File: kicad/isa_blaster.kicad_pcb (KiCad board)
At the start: 2 copper layers, 81.3 x 30.9 mm, 18 parts, among them J1 Bus_ISA_8bit, J2 Conn_02x06_Odd_Even, J3 USB_A, U3 TXS0108EPW, U4 TXS0108EPW, U5 TXS0108EPW, U6 RaspberryPi_Pico

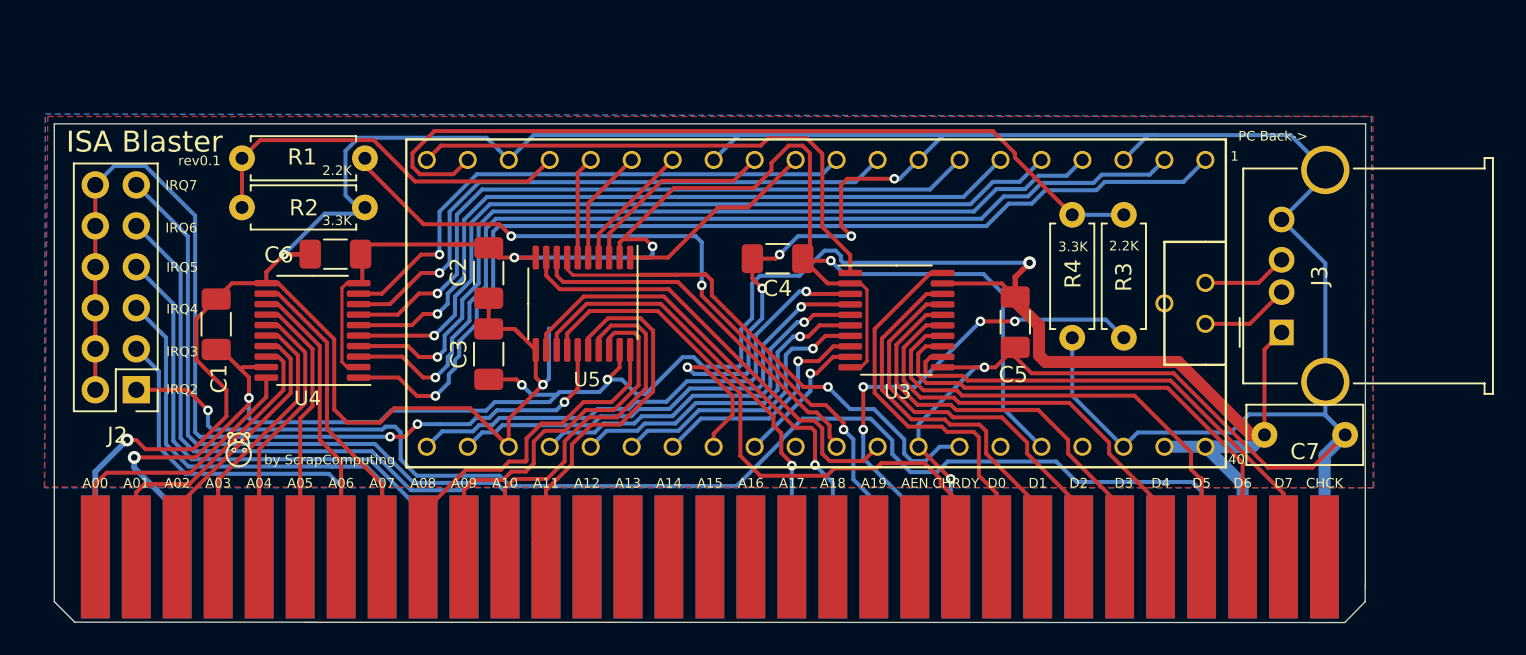
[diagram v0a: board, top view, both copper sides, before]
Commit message: Added RESET circuit, debug header and SMD resistors
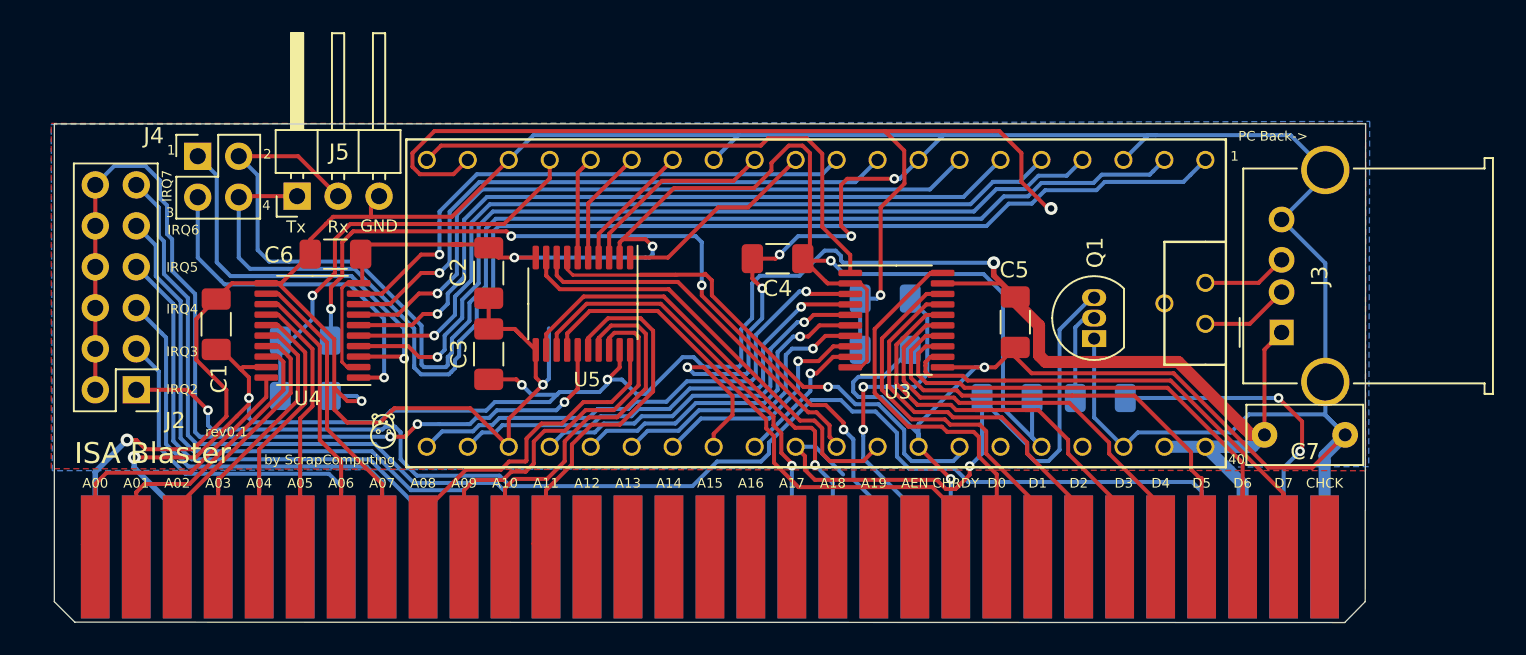
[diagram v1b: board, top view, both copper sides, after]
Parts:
- added ?: , , F.Cu at (143.5, 55.2)
- added J4: Conn_02x02_Odd_Even, Connector_PinHeader_2.54mm:PinHeader_2x02_P2.54mm_Vertical, F.Cu at (144.0, 50.7)
- added J5: Conn_01x03, Connector_PinHeader_2.54mm:PinHeader_1x03_P2.54mm_Horizontal, F.Cu at (150.2, 53.1)
- added Q1: 2N3904, Package_TO_SOT_THT:TO-92_Inline, F.Cu at (199.6, 62.0)
- added R5: 2.2K, Resistor_SMD:R_1206_3216Metric_Pad1.30x1.75mm_HandSolder, B.Cu at (194.2, 65.7)
- added R6: 3.3K, Resistor_SMD:R_1206_3216Metric_Pad1.30x1.75mm_HandSolder, B.Cu at (200.0, 65.7)
- R1, R2, R3, R4: footprint Resistor_THT:R_Axial_DIN0207_L6.3mm_D2.5mm_P7.62mm_Horizontal -> Resistor_SMD:R_1206_3216Metric_Pad1.30x1.75mm_HandSolder; moved to B.Cu
- moved R3 15.0 mm to (186.6, 59.5), turned to 180 degrees
- moved R4 14.3 mm to (186.6, 62.7), turned to 0 degrees
- moved R2 12.3 mm to (150.7, 65.5)
- moved R1 11.9 mm to (150.7, 62.1)
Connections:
- J1 pad 2: (no net) -> Net-(J1-Pad2)
- U4 pad 1: Net-(U4-Pad1) -> Net-(J4-Pad3)
- U4 pad 3: Net-(U4-Pad3) -> Net-(J4-Pad1)
- U6 pad 1: Net-(U4-Pad1) -> Net-(J4-Pad4)
- U6 pad 2: Net-(U4-Pad3) -> Net-(J4-Pad2)
- U6 pad 30: (no net) -> Net-(Q1-Pad3)
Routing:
- net Net-(J4-Pad2): track 0.00 -> 83.0 mm
- net Net-(J4-Pad4): track 0.00 -> 81.0 mm
- net Net-(U4-Pad1): track 63.2 -> 0.00 mm, vias 1 -> 0
- net Net-(U4-Pad3): track 59.6 -> 0.00 mm, vias 1 -> 0
- net Net-(Q1-Pad3): track 0.00 -> 39.9 mm, vias 0 -> 1
- net Net-(J4-Pad1): track 0.00 -> 25.1 mm, vias 0 -> 1
- net Net-(J4-Pad3): track 0.00 -> 22.1 mm, vias 0 -> 1
- net Net-(J1-Pad2): track 0.00 -> 20.6 mm, vias 0 -> 2
- net Net-(R3-Pad2): track 51.8 -> 63.8 mm, vias 0 -> 2
- net Net-(J1-Pad11): track 30.2 -> 21.3 mm, vias 4 -> 2
- net GND: track 282.9 -> 290.6 mm
- net Net-(J1-Pad12): track 47.4 -> 53.7 mm, vias 3 -> 4
- net Net-(Q1-Pad2): track 0.00 -> 5.78 mm
- net Net-(R1-Pad2): track 24.3 -> 27.9 mm, vias 0 -> 1
- net +3V3: track 89.0 -> 92.3 mm
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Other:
- board text added: "1"
- board text added: "1-2,3-4"
- board text added: "2"
- board text added: "3"
- board text added: "4"
- board text added: "Close"
- board text added: "DEBUG"
- board text added: "GND"
- board text added: "J4"
- board text added: "NORMAL"
- board text added: "Open"
- board text added: "Rx"
- board text added: "Serial Debug"
- board text added: "Tx"
